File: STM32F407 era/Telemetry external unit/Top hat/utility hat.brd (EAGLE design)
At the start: 65 x 56 mm, 22 parts, among them U1 EEPROM24, U2 SC18IM700IPW,112

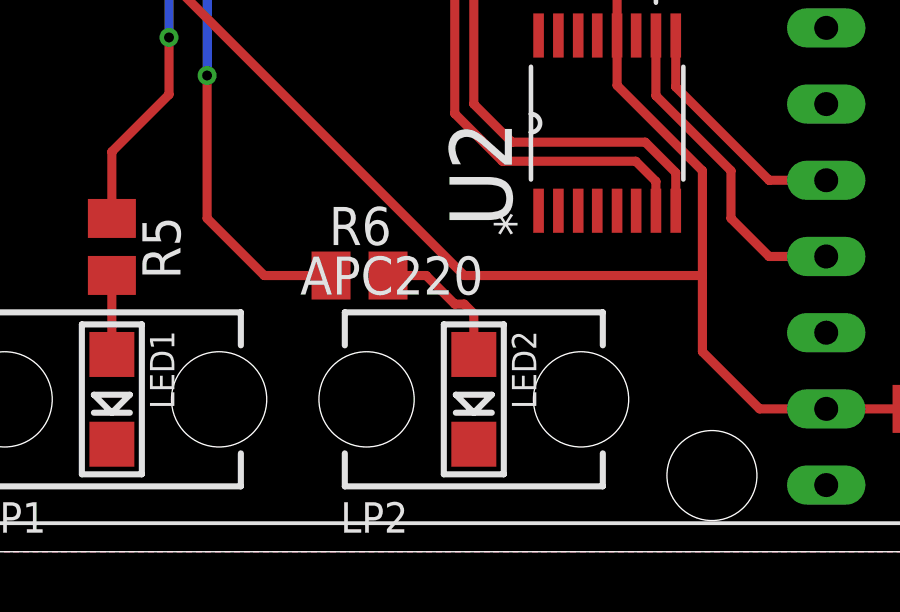
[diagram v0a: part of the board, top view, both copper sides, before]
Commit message: changes to battery board
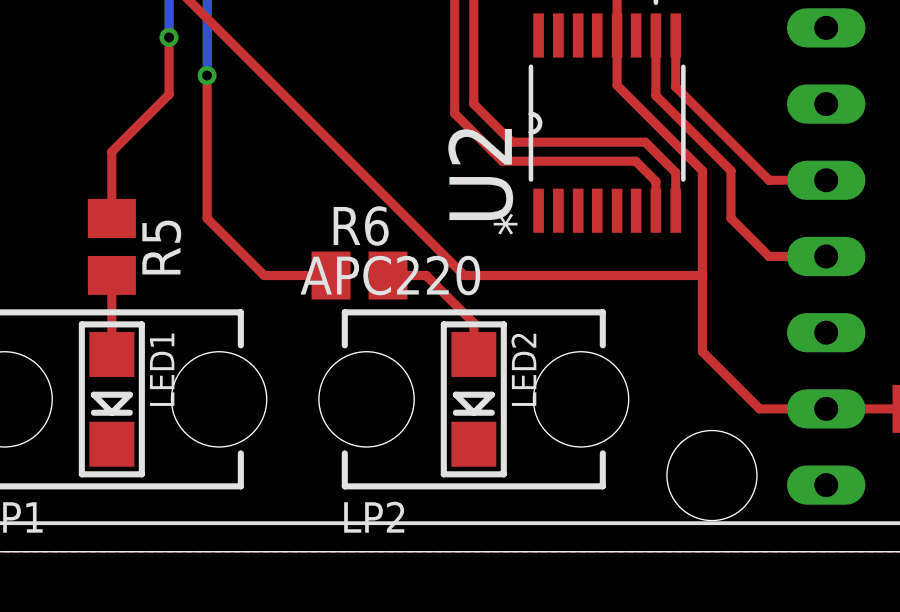
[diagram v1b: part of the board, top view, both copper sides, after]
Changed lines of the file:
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@@
 <contactref element="R6" pad="2"/>
 <contactref element="LED2" pad="A"/>
-<wire x1="26.67" y1="6.576" x2="26.67" y2="7.9375" width="0.3048" layer="1"/>
-<wire x1="26.67" y1="7.9375" x2="26.3525" y2="8.255" width="0.3048" layer="1"/>
-<wire x1="26.3525" y1="8.255" x2="26.035" y2="8.255" width="0.3048" layer="1"/>
-<wire x1="26.035" y1="8.255" x2="25.0825" y2="9.2075" width="0.3048" layer="1"/>
+<wire x1="26.67" y1="6.576" x2="26.67" y2="7.62" width="0.3048" layer="1"/>
+<wire x1="26.67" y1="7.62" x2="25.0825" y2="9.2075" width="0.3048" layer="1"/>
 <wire x1="25.0825" y1="9.2075" x2="23.81" y2="9.2075" width="0.3048" layer="1"/>
 </signal>

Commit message: Minor changes to utility hat
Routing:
- net +3V3: track 121.3 -> 120.5 mm
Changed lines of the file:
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@@
 <wire x1="30.353" y1="49.53" x2="28.702" y2="51.181" width="0.3048" layer="1"/>
 <contactref element="XB1" pad="1"/>
-<wire x1="8.382" y1="51.181" x2="8.382" y2="48.387" width="0.3048" layer="1"/>
-<wire x1="8.382" y1="48.387" x2="7.62" y2="47.625" width="0.3048" layer="1"/>
-<wire x1="7.62" y1="47.625" x2="6.35" y2="47.625" width="0.3048" layer="1"/>
-<wire x1="6.35" y1="47.625" x2="5.3975" y2="46.6725" width="0.3048" layer="1"/>
-<wire x1="5.3975" y1="46.6725" x2="5.3975" y2="26.3525" width="0.3048" layer="1"/>
+<wire x1="8.382" y1="51.181" x2="7.112" y2="49.9745" width="0.3048" layer="1"/>
+<wire x1="7.112" y1="49.9745" x2="5.3975" y2="48.26" width="0.3048" layer="1"/>
+<wire x1="5.3975" y1="48.26" x2="5.3975" y2="26.3525" width="0.3048" layer="1"/>
 <wire x1="5.3975" y1="25.085" x2="6.5575" y2="23.925" width="0.3048" layer="1"/>
 <contactref element="U$1" pad="VCC"/>
@@
 <wire x1="13.462" y1="49.403" x2="13.6525" y2="49.2125" width="0.3048" layer="1"/>
 <via x="13.6525" y="49.2125" extent="1-16" drill="0.3302"/>
-<wire x1="13.6525" y1="49.2125" x2="16.51" y2="49.2125" width="0.3048" layer="16"/>
-<wire x1="16.51" y1="49.2125" x2="16.8275" y2="48.895" width="0.3048" layer="16"/>
-<via x="16.8275" y="48.895" extent="1-16" drill="0.3302"/>
+<wire x1="13.6525" y1="49.2125" x2="16.8275" y2="49.2125" width="0.3048" layer="16"/>
+<wire x1="16.8275" y1="49.2125" x2="17.145" y2="48.895" width="0.3048" layer="16"/>
+<via x="17.145" y="48.895" extent="1-16" drill="0.3302"/>
 <wire x1="26.67" y1="14.9225" x2="27.94" y2="13.6525" width="0.3048" layer="1"/>
 <wire x1="27.94" y1="13.6525" x2="32.385" y2="13.6525" width="0.3048" layer="1"/>
 <wire x1="32.385" y1="13.6525" x2="33.401" y2="12.6365" width="0.3048" layer="1"/>
 <wire x1="33.401" y1="12.6365" x2="33.401" y2="11.3665" width="0.3048" layer="1"/>
-<wire x1="16.8275" y1="48.895" x2="18.415" y2="47.3075" width="0.3048" layer="1"/>
-<wire x1="18.415" y1="47.3075" x2="18.7325" y2="47.3075" width="0.3048" layer="1"/>
-<wire x1="18.7325" y1="47.3075" x2="19.558" y2="46.482" width="0.3048" layer="1"/>
+<wire x1="17.145" y1="48.895" x2="19.558" y2="46.482" width="0.3048" layer="1"/>
 <wire x1="20.32" y1="26.3525" x2="26.035" y2="26.3525" width="0.3048" layer="1"/>
 <wire x1="26.035" y1="26.3525" x2="26.67" y2="25.7175" width="0.3048" layer="1"/>

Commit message: added 5-way CAN splitter and continued work
more work have been done one the laptimer layout
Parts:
- removed U$1: APC220, APC220:APC220
- added XB2: XBEE-PRO, maxstream:XBEE-PRO
- moved LED1 81.4 mm to (94.6, 20.3)
- moved LP1 81.4 mm to (94.6, 20.3)
- moved R5 81.4 mm to (94.6, 25.4)
- moved R6 51.8 mm to (74.0, 17.8)
- moved U2 51.8 mm to (82.2, 22.9)
- moved C2 51.8 mm to (81.6, 28.3)
- moved LED2 51.8 mm to (77.8, 13.7)
- moved LP2 51.8 mm to (77.8, 13.7)
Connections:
- new net VCC: XB2.1
- net +3V3: now also XB2.5; no longer U$1.VCC
- net GND: now also XB2.10; no longer U$1.GND
- net N$1: now also XB2.3; no longer U$1.RXD
- net N$2: now also XB2.2; no longer U$1.TXD
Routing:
- net +3V3: track 120.5 -> 61.7 mm
- net SCL: track 55.9 -> 36.1 mm
- net SDA: track 58.2 -> 38.7 mm
- net N$5: track 40.2 -> 21.5 mm, vias 2 -> 0
- net N$7: track 13.7 -> 0.00 mm, vias 2 -> 0
- net N$1: track 10.8 -> 0.00 mm
- net N$2: track 8.02 -> 0.00 mm
- net N$6: track 4.56 -> 0.00 mm
- net N$8: track 2.63 -> 0.00 mm

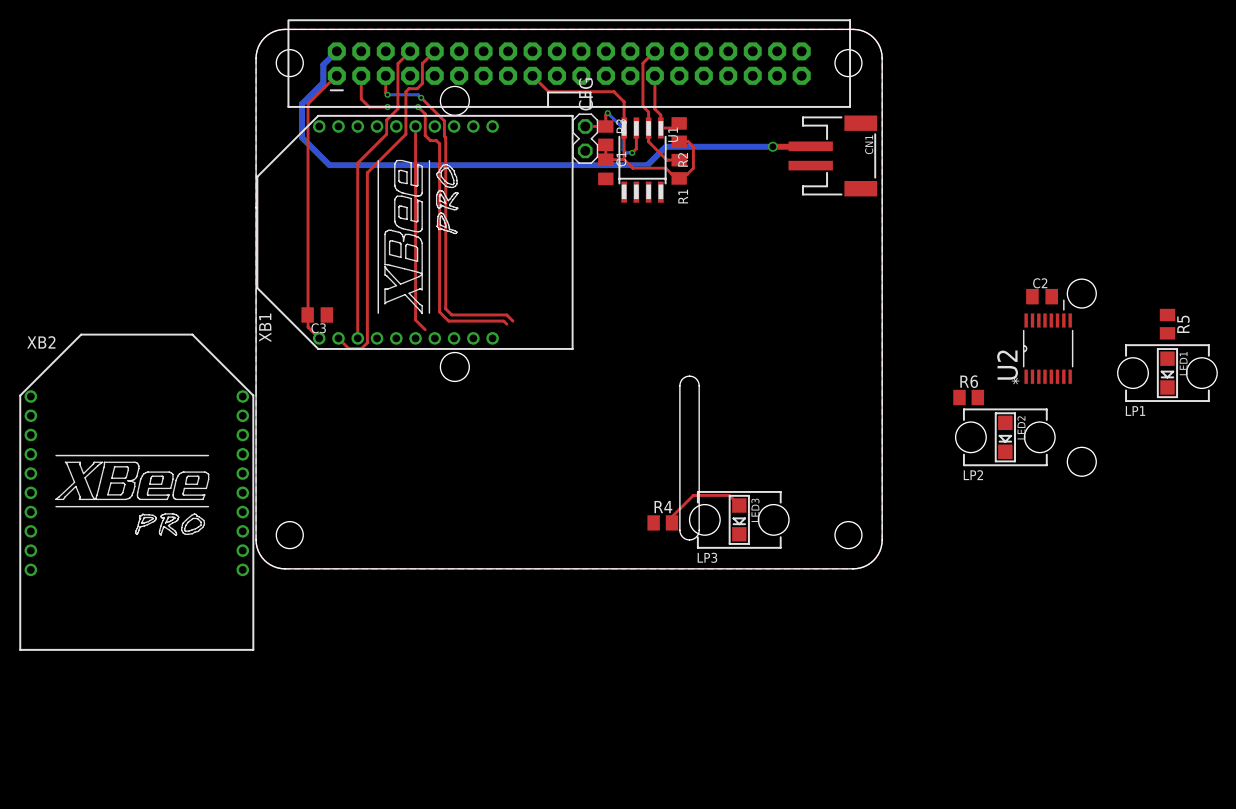
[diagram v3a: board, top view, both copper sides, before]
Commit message: layout updates to fit 2 xbees
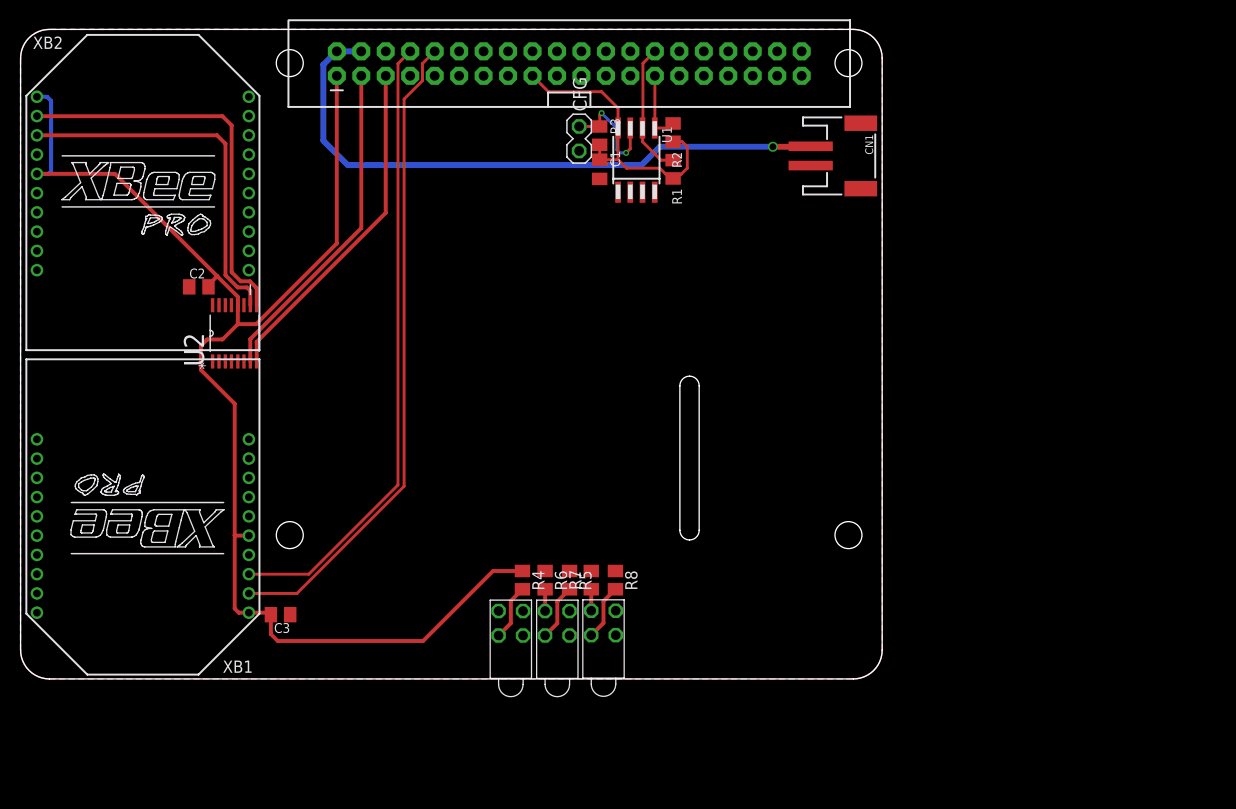
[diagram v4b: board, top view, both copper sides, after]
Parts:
- removed LED1, LED2, LED3: (no value), microbuilder:CHIPLED_1206
- removed LP1, LP2, LP3: LPF-C011304S, light-pipe:LPF-C011304S
- added R7, R8: 3k9, resistor:M0805
- added U$1, U$2, U$3: BI-LEVEL-LED-INDICATOR, unicorn_v2:BI-LEVEL-LED-INDICATOR
- moved C2 87.5 mm to (-5.94, 29.3)
- moved U2 84.5 mm to (-2.22, 24.4)
- moved R5 67.5 mm to (32.5, -1.17)
- moved R6 47.9 mm to (30.0, -1.17), turned to 270 degrees
- moved XB1 40.9 mm to (-11.7, 4.45), turned to 180 degrees
- moved C3 31.3 mm to (2.54, -4.76)
- moved XB2 31.1 mm to (-11.7, 40.0)
- moved R4 15.7 mm to (27.7, -1.17), turned to 270 degrees
- moved R1 0.64 mm to (43.3, 41.5)
- moved R2 0.64 mm to (43.3, 45.3)
- moved C1 0.63 mm to (35.7, 41.5)
- moved CFG 0.63 mm to (33.5, 45.9)
- moved R3 0.63 mm to (35.7, 45.0)
- moved U1 0.63 mm to (39.5, 42.4)
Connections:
- removed net VCC: XB2.1
- new net N$10: R8.2, U$2.ANODE1
- new net N$11: R7.2, XB2.15
- new net N$12: R8.1, XB2.6
- new net N$9: R7.1, U$2.ANODE2
- net +3V3: now also XB2.1
- net GND: now also U$1.CATHODE1, U$1.CATHODE2, U$2.CATHODE1, U$2.CATHODE2, U$3.CATHODE1, U$3.CATHODE2; no longer LED1.C, LED2.C, LED3.C
- net N$4: now also U$3.ANODE1; no longer LED3.A
- net N$6: now also U$1.ANODE2; no longer LED2.A
- net N$8: now also U$1.ANODE1; no longer LED1.A
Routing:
- net +3V3: track 61.7 -> 174.3 mm
- net N$2: track 0.00 -> 40.9 mm
- net N$1: track 0.00 -> 38.3 mm
- net TX: track 32.1 -> 64.9 mm
- net RX: track 37.3 -> 67.2 mm
- net N$5: track 21.5 -> 0.00 mm
- net N$8: track 0.00 -> 5.85 mm
- net N$10: track 0.00 -> 5.80 mm
- net SDA: track 38.7 -> 34.4 mm, vias 2 -> 0
- net N$4: track 8.97 -> 5.82 mm
- net N$6: track 0.00 -> 2.26 mm
- net N$9: track 0.00 -> 2.23 mm
- net SCL: track 36.1 -> 35.2 mm, vias 2 -> 0
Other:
- board size 65 x 56 mm -> 89.4 x 67.4 mm

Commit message: library updates and layout updates
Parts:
- removed C1, C3: 100nF, resistor:C0805K
- removed CFG: (no value), FLYFISH:PIN_W_2
- removed R1, R2: 3k9, resistor:M0805
- removed R3: 1k, resistor:M0805
- removed U1: EEPROM24, FLYFISH:SOIC8
- flipped R4 to the bottom
- flipped R5 to the bottom
- flipped R6 to the bottom
- flipped R7 to the bottom
- flipped R8 to the bottom
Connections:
- removed net N$3: CFG.1, R3.1, U1.7
- net +3V3: no longer C1.1, C3.2, R1.2, R2.2, R3.2, U1.8
- net GND: no longer C1.2, C3.1, CFG.2, U1.1, U1.2, U1.3, U1.4
- net ID_SC: no longer R1.1, U1.6
- net ID_SD: no longer R2.1, U1.5
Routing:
- net N$12: track 0.00 -> 87.5 mm
- net N$11: track 0.00 -> 66.5 mm, vias 0 -> 2
- net N$5: track 0.00 -> 66.3 mm, vias 0 -> 2
- net N$7: track 0.00 -> 38.1 mm
- net +3V3: track 174.3 -> 143.2 mm, vias 0 -> 3
- net ID_SC: track 13.9 -> 0.00 mm
- net N$3: track 11.9 -> 0.00 mm, vias 2 -> 0
- net ID_SD: track 7.68 -> 0.00 mm
- net +5V: track 64.8 -> 63.6 mm, vias 1 -> 2
- net TX: vias 0 -> 1
- net N$1: track 38.3 -> 38.4 mm, vias 0 -> 1
- net RX: vias 0 -> 1
- net N$2: vias 0 -> 1

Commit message: layout updates
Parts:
- moved U$2 1.59 mm to (36.1, -7.21)
- moved XB1 1.59 mm to (-11.7, 2.86)
- moved R4 1.59 mm to (27.7, -2.76)
- moved R5 1.59 mm to (32.5, -2.76)
- moved R6 1.59 mm to (30.0, -2.76)
- moved R7 1.59 mm to (34.8, -2.76)
- moved R8 1.59 mm to (37.3, -2.76)
- moved U$1 1.59 mm to (31.3, -7.24)
- moved U$3 1.59 mm to (26.4, -7.24)
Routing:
- net +3V3: track 143.2 -> 148.6 mm
- net RX: track 67.2 -> 68.8 mm
- net N$12: track 87.5 -> 89.1 mm
- net N$11: track 66.5 -> 68.1 mm
- net N$7: track 38.1 -> 39.5 mm
- net TX: track 64.9 -> 65.8 mm
- net N$5: track 66.3 -> 66.8 mm
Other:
- board size 89.4 x 67.4 mm -> 89.4 x 69 mm

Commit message: preperations for etching
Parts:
- added U$4, U$5: MOUNTINGHOLE3.0THIN, microbuilder:MOUNTINGHOLE_3.0_PLATEDTHIN

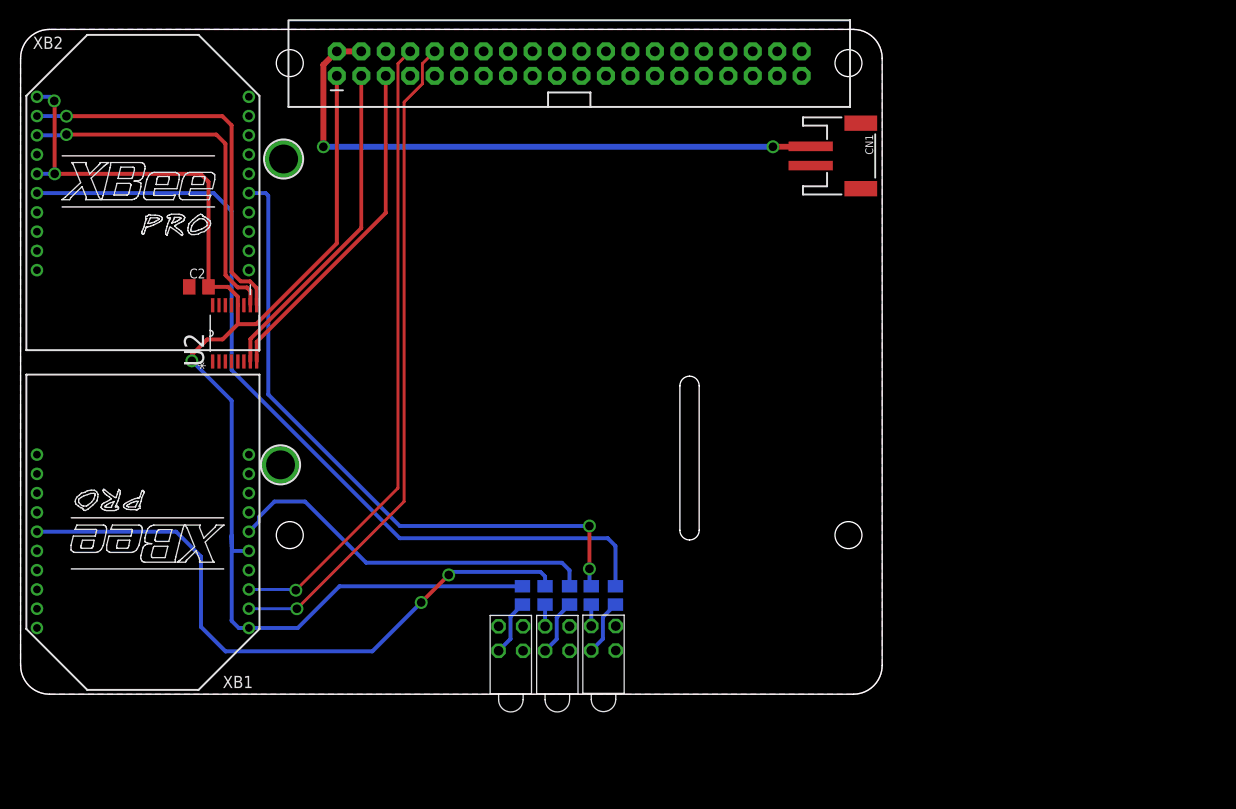
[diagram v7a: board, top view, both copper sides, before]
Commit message: layout update, and added power switch
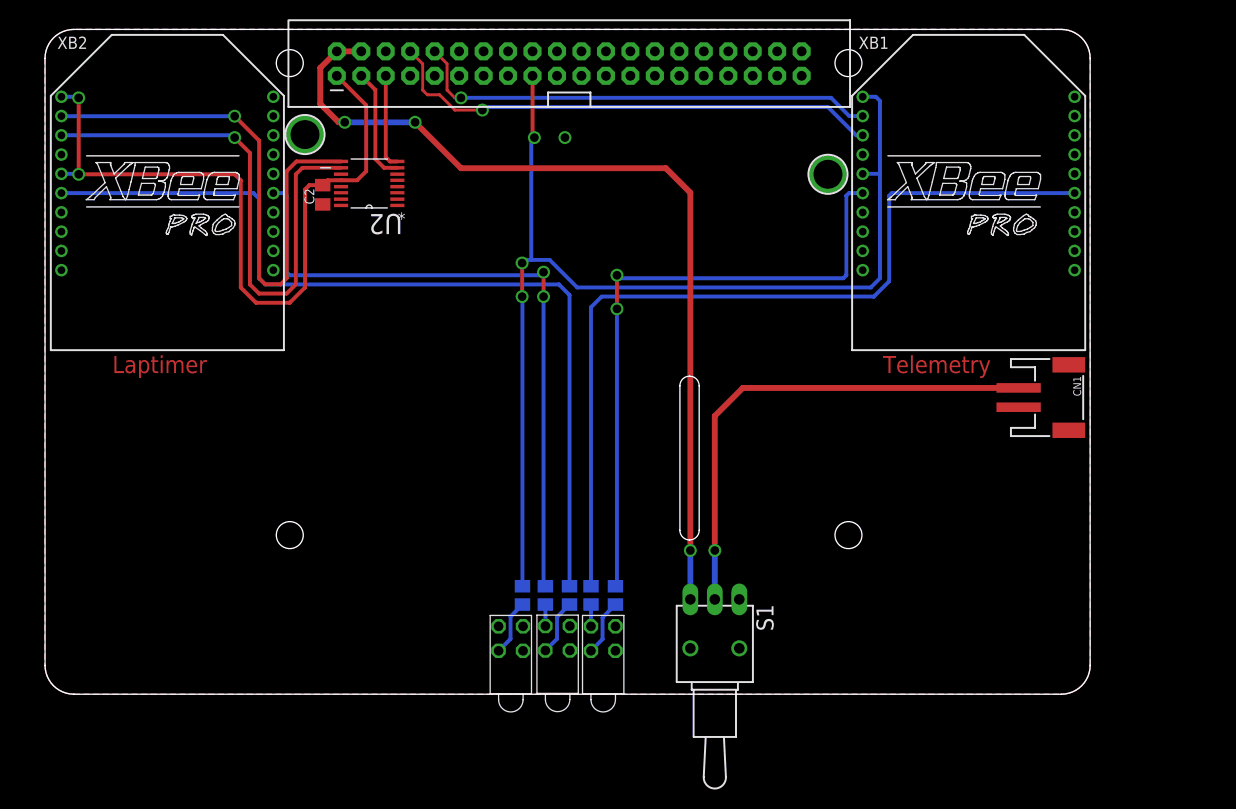
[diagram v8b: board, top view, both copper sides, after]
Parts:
- added S1: TL36WO, switch:TL3XWO
- moved XB1 93.4 mm to (74.0, 40.0), turned to 0 degrees
- moved U$4 56.5 mm to (59.4, 41.0)
- moved U$5 34.4 mm to (5.08, 45.1)
- moved CN1 33.1 mm to (82.9, 17.8)
- moved U2 20.9 mm to (11.7, 40.0), turned to 180 degrees
- moved C2 16.0 mm to (6.92, 38.8), turned to 90 degrees
- moved R7 4.76 mm to (30.0, -2.76)
- moved U$1 4.76 mm to (36.0, -7.24)
- moved R6 4.76 mm to (34.8, -2.76)
- moved U$2 4.76 mm to (31.3, -7.21)
- moved R5 4.76 mm to (37.3, -2.76)
- moved R8 4.76 mm to (32.5, -2.76)
- moved XB2 2.54 mm to (-9.21, 40.0)
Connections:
- removed net ID_SC: JP1.28
- removed net ID_SD: JP1.27
- new net N$16: CN1.1, S1.2
- net +5V: now also S1.3; no longer CN1.1
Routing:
- net N$16: track 0.00 -> 51.8 mm, vias 0 -> 1
- net +3V3: track 148.6 -> 190.2 mm, vias 3 -> 5
- net +5V: track 63.6 -> 93.2 mm, vias 2 -> 3
- net N$7: track 39.5 -> 66.5 mm, vias 0 -> 2
- net SCL: track 35.2 -> 9.84 mm
- net SDA: track 34.4 -> 11.9 mm
- net N$5: track 66.8 -> 89.3 mm, vias 2 -> 0
- net RX: track 68.8 -> 48.8 mm
- net N$1: track 38.4 -> 55.9 mm
- net N$2: track 40.9 -> 56.4 mm
- net TX: track 65.8 -> 52.4 mm
- net N$12: track 89.1 -> 92.2 mm
- net N$11: track 68.1 -> 69.1 mm
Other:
- board size 89.4 x 69 mm -> 108.5 x 69 mm
- board text added: "Laptimer"
- board text added: "Telemetry"
